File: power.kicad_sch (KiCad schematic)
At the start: 8 parts

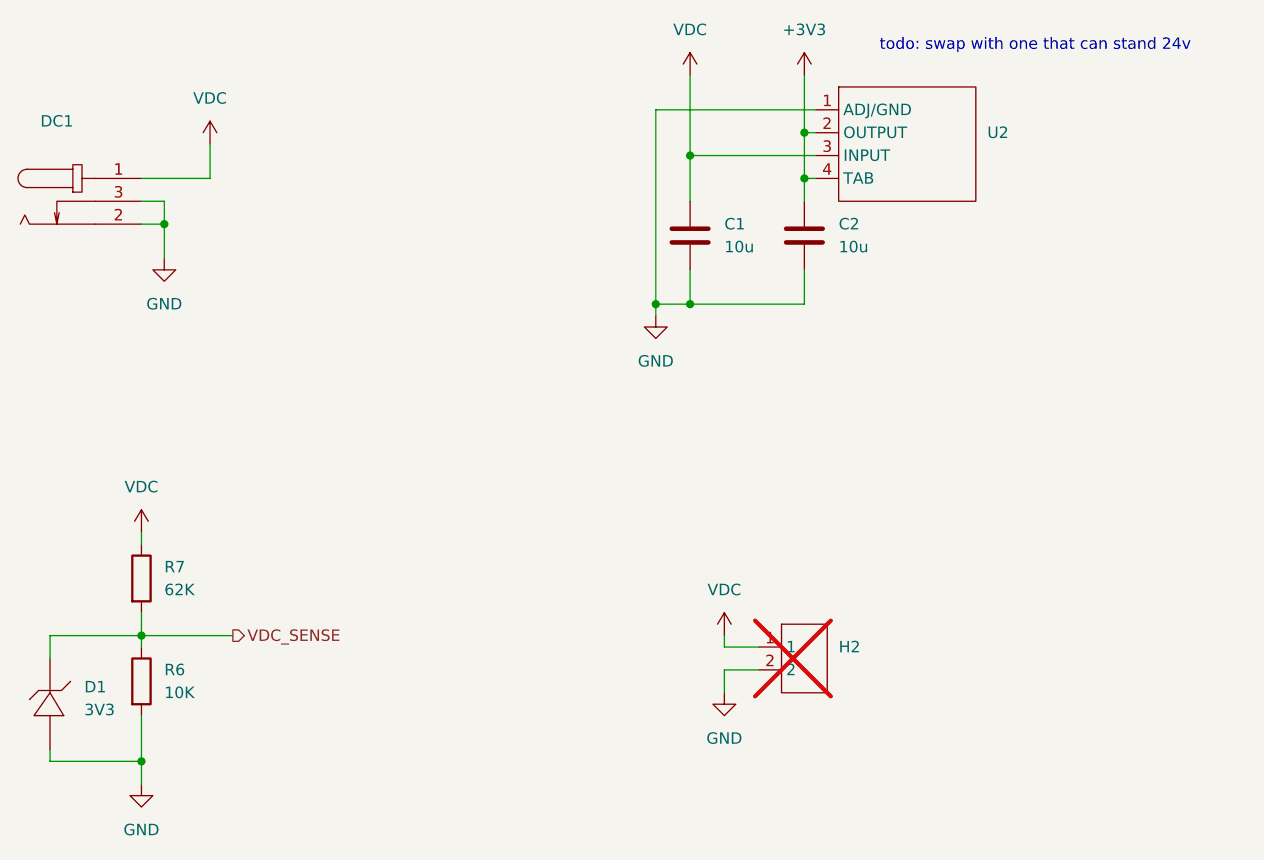
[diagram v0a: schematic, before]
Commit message: Finished schematics, started component placement
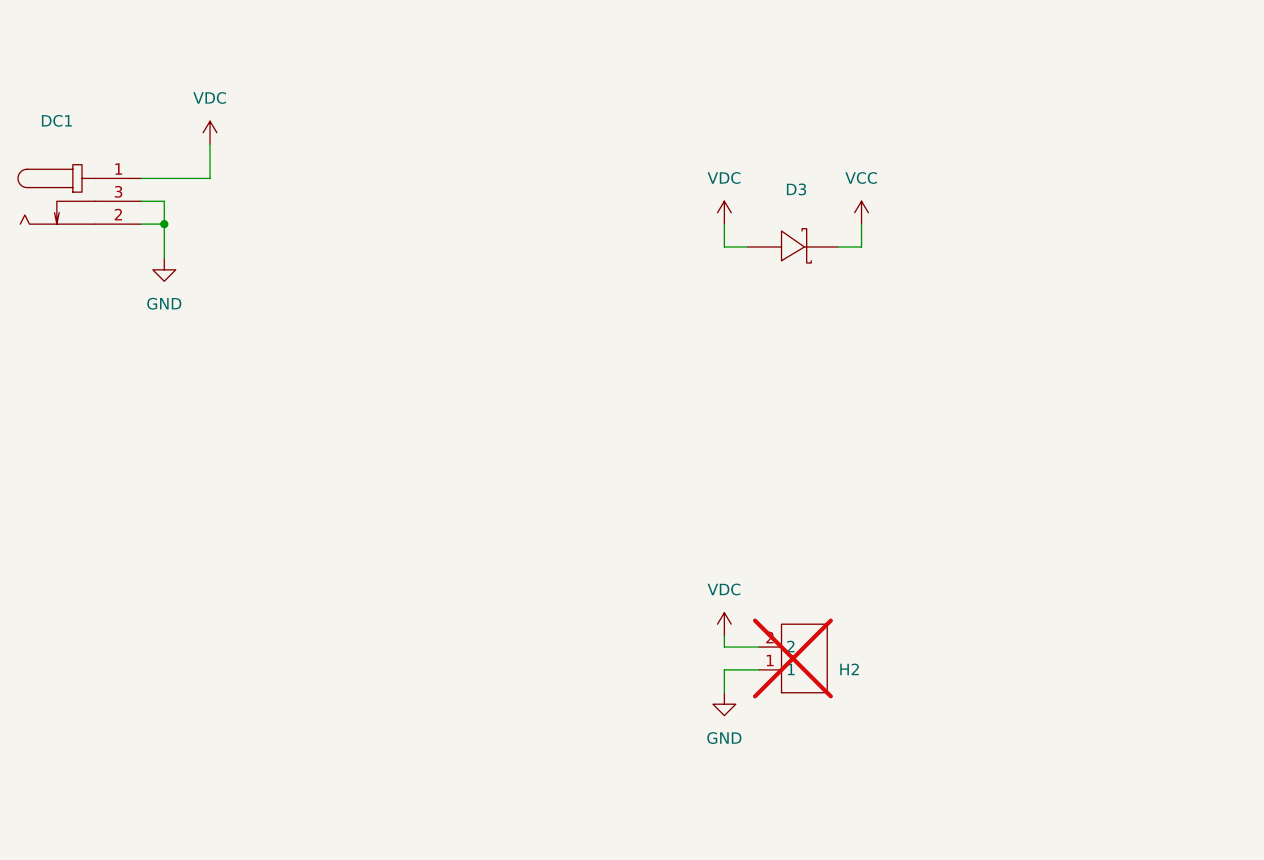
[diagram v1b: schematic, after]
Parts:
- removed C1, C2: 10u, Capacitor_SMD:C_0603_1608Metric, symbol Device:C
- removed D1: 3V3, EasyEDA_Lib:SOD-123_L2.7-W1.6-LS3.7-RD, symbol EasyEDA_Lib:BZT52C3V3
- removed R6: 10K, Resistor_SMD:R_0603_1608Metric, symbol Device:R
- removed R7: 62K, Resistor_SMD:R_0603_1608Metric, symbol Device:R
- removed U2: ~, EasyEDA_Lib:SOT-223-3_L6.5-W3.4-P2.30-LS7.0-BR, symbol EasyEDA_Lib:NCP1117ST33T3G
- added D3: ~, EasyEDA_Lib:SMA_L4.4-W2.6-LS5.0-RD, symbol EasyEDA_Lib:B340A-13-F
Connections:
- net GND: now also H2.1; no longer H2.2
- net VDC: now also H2.2, D3.2 (A); no longer H2.1
- new net VCC: D3.1 (K)
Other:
- note removed: "todo: swap with one that can stand 24v"
